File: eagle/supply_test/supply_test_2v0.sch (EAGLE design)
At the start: 46 parts, among them J1 SOCKET, J10 SOCKET, J11 SOCKET, J12 SOCKET, J13 SOCKET, J14 SOCKET, J15 SOCKET, J16 SOCKET, J17 SOCKET, J18 SOCKET, J19 SOCKET, J2 SOCKET, J20 SOCKET, J21 AC_INSW, J22 SOCKET, J23 MA02-1STR, J3 SOCKET, J4 SOCKET, J5 SOCKET, J6 SOCKET, J7 SOCKET, J8 SOCKET, J9 SOCKET

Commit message: supply test version 2
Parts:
- removed C4: (no value), rcl:C-EUC0603
- removed D4: ZENERBZT52, powerfilm:ZENERBZT52
- removed J23: MA02-1STR, con-lstb:MA02-1STR
- removed R7: 1k, rcl:R-US_R0603
- removed TP3: TP_STD, skyspecs:TP_STD
- added U1: TPS62122, powerfilm:TPS62122
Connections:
- removed net N$10: C4.1, D4.C, R7.2, TP3.P$1
- removed net N$9: J23.2, R7.1
- net GND: no longer C4.2, D4.A
- net VCC: no longer J23.1

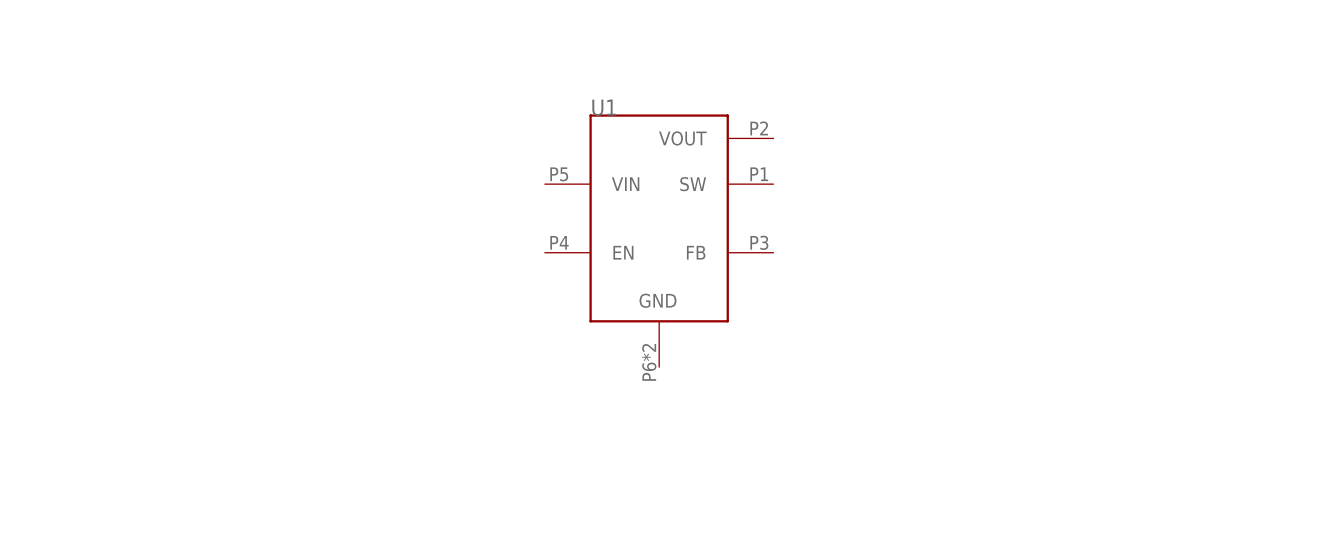
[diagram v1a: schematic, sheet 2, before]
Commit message: added different regulator to supply test
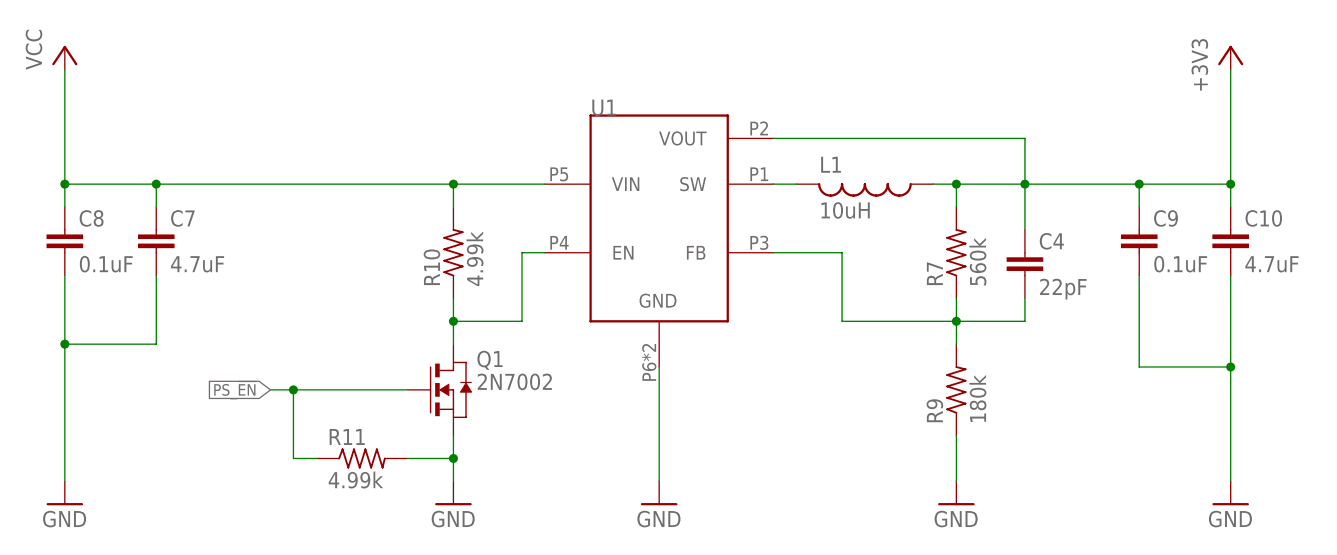
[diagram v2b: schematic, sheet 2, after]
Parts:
- added C10, C7: 4.7uF, rcl:C-EUC0603
- added C4: 22pF, rcl:C-EUC0603
- added C8, C9: 0.1uF, rcl:C-EUC0603
- added L1: 10uH, rcl:L-USL0805
- added Q1: 2N7002, nav:2N7002
- added R10, R11: 4.99k, rcl:R-US_R0603
- added R7: 560k, rcl:R-US_R0603
- added R9: 180k, rcl:R-US_R0603
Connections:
- new net +3V3: C10.1, C4.1, C9.1, L1.1, R7.2, U1.VOUT
- new net N$13: C4.2, R7.1, R9.2, U1.FB
- new net N$16: Q1.D, R10.1, U1.EN
- new net N$9: L1.2, U1.SW
- new net PS_!EN!: Q1.G, R11.1
- net GND: now also C10.2, C7.2, C8.2, C9.2, Q1.S, R11.2, R9.1, U1.GND
- net VCC: now also C7.1, C8.1, R10.2, U1.VIN
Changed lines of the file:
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@@
 <?xml version="1.0" encoding="utf-8"?>
 <!DOCTYPE eagle SYSTEM "eagle.dtd">
-<eagle version="6.5.0">
+<eagle version="6.3">
 <drawing>
 <settings>
@@
 </part>
 <part name="U1" library="powerfilm" deviceset="TPS62122" device=""/>
+<part name="L1" library="rcl" deviceset="L-US" device="L0805" value="10uH">
+<attribute name="DIGIKEY" value="490-4990-1-ND"/>
+</part>
+<part name="R7" library="rcl" deviceset="R-US_" device="R0603" value="560k"/>
+<part name="R9" library="rcl" deviceset="R-US_" device="R0603" value="180k"/>
+<part name="GND3" library="supply1" deviceset="GND" device=""/>
+<part name="GND4" library="supply1" deviceset="GND" device=""/>
+<part name="C4" library="rcl" deviceset="C-EU" device="C0603" value="22pF"/>
+<part name="R10" library="rcl" deviceset="R-US_" device="R0603" value="4.99k"/>
+<part name="Q1" library="nav" deviceset="2N7002" device=""/>
+<part name="GND5" library="supply1" deviceset="GND" device=""/>
+<part name="R11" library="rcl" deviceset="R-US_" device="R0603" value="4.99k"/>
+<part name="+3V1" library="supply1" deviceset="+3V3" device=""/>
+<part name="P+2" library="supply1" deviceset="VCC" device=""/>
+<part name="C7" library="rcl" deviceset="C-EU" device="C0603" value="4.7uF"/>
+<part name="C8" library="rcl" deviceset="C-EU" device="C0603" value="0.1uF"/>
+<part name="C9" library="rcl" deviceset="C-EU" device="C0603" value="0.1uF"/>
+<part name="C10" library="rcl" deviceset="C-EU" device="C0603" value="4.7uF"/>
+<part name="GND6" library="supply1" deviceset="GND" device=""/>
+<part name="GND7" library="supply1" deviceset="GND" device=""/>
 </parts>
 <sheets>
@@
 <instances>
 <instance part="U1" gate="G$1" x="0" y="0"/>
+<instance part="L1" gate="G$1" x="22.86" y="5.08" rot="R270">
+<attribute name="DIGIKEY" x="22.86" y="5.08" size="1.27" layer="96" rot="R270" display="off"/>
+</instance>
+<instance part="R7" gate="G$1" x="33.02" y="-2.54" rot="R90"/>
+<instance part="R9" gate="G$1" x="33.02" y="-17.78" rot="R90"/>
+<instance part="GND3" gate="1" x="33.02" y="-30.48"/>
+<instance part="GND4" gate="1" x="0" y="-30.48"/>
+<instance part="C4" gate="G$1" x="40.64" y="-2.54"/>
+<instance part="R10" gate="G$1" x="-22.86" y="-2.54" rot="R90"/>
+<instance part="Q1" gate="G$1" x="-22.86" y="-17.78"/>
+<instance part="GND5" gate="1" x="-22.86" y="-30.48"/>
+<instance part="R11" gate="G$1" x="-33.02" y="-25.4"/>
+<instance part="+3V1" gate="G$1" x="63.5" y="20.32"/>
+<instance part="P+2" gate="VCC" x="-66.04" y="20.32"/>
+<instance part="C7" gate="G$1" x="-55.88" y="0"/>
+<instance part="C8" gate="G$1" x="-66.04" y="0"/>
+<instance part="C9" gate="G$1" x="53.34" y="0"/>
+<instance part="C10" gate="G$1" x="63.5" y="0"/>
+<instance part="GND6" gate="1" x="-66.04" y="-30.48"/>
+<instance part="GND7" gate="1" x="63.5" y="-30.48"/>
 </instances>
 <busses>
 </busses>
 <nets>
+<net name="N$13" class="0">
+<segment>
+<pinref part="U1" gate="G$1" pin="FB"/>
+<wire x1="12.7" y1="-2.54" x2="20.32" y2="-2.54" width="0.1524" layer="91"/>
+<wire x1="20.32" y1="-2.54" x2="20.32" y2="-10.16" width="0.1524" layer="91"/>
+<pinref part="R7" gate="G$1" pin="1"/>
+<wire x1="20.32" y1="-10.16" x2="33.02" y2="-10.16" width="0.1524" layer="91"/>
+<wire x1="33.02" y1="-10.16" x2="33.02" y2="-7.62" width="0.1524" layer="91"/>
+<pinref part="R9" gate="G$1" pin="2"/>
+<wire x1="33.02" y1="-10.16" x2="33.02" y2="-12.7" width="0.1524" layer="91"/>
+<junction x="33.02" y="-10.16"/>
+<pinref part="C4" gate="G$1" pin="2"/>
+<wire x1="33.02" y1="-10.16" x2="40.64" y2="-10.16" width="0.1524" layer="91"/>
+<wire x1="40.64" y1="-10.16" x2="40.64" y2="-7.62" width="0.1524" layer="91"/>
+</segment>
+</net>
+<net name="GND" class="0">
+<segment>
+<pinref part="R9" gate="G$1" pin="1"/>
+<pinref part="GND3" gate="1" pin="GND"/>
+<wire x1="33.02" y1="-22.86" x2="33.02" y2="-27.94" width="0.1524" layer="91"/>
+</segment>
+<segment>
+<pinref part="U1" gate="G$1" pin="GND"/>
+<pinref part="GND4" gate="1" pin="GND"/>
+<wire x1="0" y1="-15.24" x2="0" y2="-27.94" width="0.1524" layer="91"/>
+</segment>
+<segment>
+<pinref part="Q1" gate="G$1" pin="S"/>
+<pinref part="GND5" gate="1" pin="GND"/>
+<wire x1="-22.86" y1="-22.86" x2="-22.86" y2="-25.4" width="0.1524" layer="91"/>
+<pinref part="R11" gate="G$1" pin="2"/>
+<wire x1="-22.86" y1="-25.4" x2="-22.86" y2="-27.94" width="0.1524" layer="91"/>
+<wire x1="-27.94" y1="-25.4" x2="-22.86" y2="-25.4" width="0.1524" layer="91"/>
+<junction x="-22.86" y="-25.4"/>
+</segment>
+<segment>
+<pinref part="C8" gate="G$1" pin="2"/>
+<pinref part="GND6" gate="1" pin="GND"/>
+<wire x1="-66.04" y1="-5.08" x2="-66.04" y2="-12.7" width="0.1524" layer="91"/>
+<pinref part="C7" gate="G$1" pin="2"/>
+<wire x1="-66.04" y1="-12.7" x2="-66.04" y2="-27.94" width="0.1524" layer="91"/>
+<wire x1="-55.88" y1="-5.08" x2="-55.88" y2="-12.7" width="0.1524" layer="91"/>
+<wire x1="-55.88" y1="-12.7" x2="-66.04" y2="-12.7" width="0.1524" layer="91"/>
+<junction x="-66.04" y="-12.7"/>
+</segment>
+<segment>
+<pinref part="C9" gate="G$1" pin="2"/>
+<wire x1="53.34" y1="-5.08" x2="53.34" y2="-15.24" width="0.1524" layer="91"/>
+<pinref part="C10" gate="G$1" pin="2"/>
+<wire x1="53.34" y1="-15.24" x2="63.5" y2="-15.24" width="0.1524" layer="91"/>
+<wire x1="63.5" y1="-15.24" x2="63.5" y2="-5.08" width="0.1524" layer="91"/>
+<pinref part="GND7" gate="1" pin="GND"/>
+<wire x1="63.5" y1="-15.24" x2="63.5" y2="-27.94" width="0.1524" layer="91"/>
+<junction x="63.5" y="-15.24"/>
+</segment>
+</net>
+<net name="N$16" class="0">
+<segment>
+<pinref part="R10" gate="G$1" pin="1"/>
+<wire x1="-22.86" y1="-7.62" x2="-22.86" y2="-10.16" width="0.1524" layer="91"/>
+<wire x1="-22.86" y1="-10.16" x2="-15.24" y2="-10.16" width="0.1524" layer="91"/>
+<wire x1="-15.24" y1="-10.16" x2="-15.24" y2="-2.54" width="0.1524" layer="91"/>
+<pinref part="U1" gate="G$1" pin="EN"/>
+<wire x1="-15.24" y1="-2.54" x2="-12.7" y2="-2.54" width="0.1524" layer="91"/>
+<pinref part="Q1" gate="G$1" pin="D"/>
+<wire x1="-22.86" y1="-10.16" x2="-22.86" y2="-12.7" width="0.1524" layer="91"/>
+<junction x="-22.86" y="-10.16"/>
+</segment>
+</net>
+<net name="PS_!EN!" class="0">
+<segment>
+<pinref part="R11" gate="G$1" pin="1"/>
+<wire x1="-38.1" y1="-25.4" x2="-40.64" y2="-25.4" width="0.1524" layer="91"/>
+<wire x1="-40.64" y1="-25.4" x2="-40.64" y2="-17.78" width="0.1524" layer="91"/>
+<pinref part="Q1" gate="G$1" pin="G"/>
+<wire x1="-40.64" y1="-17.78" x2="-27.94" y2="-17.78" width="0.1524" layer="91"/>
+<wire x1="-43.18" y1="-17.78" x2="-40.64" y2="-17.78" width="0.1524" layer="91"/>
+<junction x="-40.64" y="-17.78"/>
+<label x="-43.18" y="-17.78" size="1.27" layer="95" rot="R180" xref="yes"/>
+</segment>
+</net>
+<net name="N$9" class="0">
+<segment>
+<pinref part="U1" gate="G$1" pin="SW"/>
+<pinref part="L1" gate="G$1" pin="2"/>
+<wire x1="12.7" y1="5.08" x2="15.24" y2="5.08" width="0.1524" layer="91"/>
+</segment>
+</net>
+<net name="VCC" class="0">
+<segment>
+<pinref part="P+2" gate="VCC" pin="VCC"/>
+<pinref part="C8" gate="G$1" pin="1"/>
+<wire x1="-66.04" y1="17.78" x2="-66.04" y2="5.08" width="0.1524" layer="91"/>
+<pinref part="U1" gate="G$1" pin="VIN"/>
+<pinref part="R10" gate="G$1" pin="2"/>
+<wire x1="-66.04" y1="5.08" x2="-66.04" y2="2.54" width="0.1524" layer="91"/>
+<wire x1="-12.7" y1="5.08" x2="-22.86" y2="5.08" width="0.1524" layer="91"/>
+<wire x1="-22.86" y1="5.08" x2="-22.86" y2="2.54" width="0.1524" layer="91"/>
+<wire x1="-22.86" y1="5.08" x2="-55.88" y2="5.08" width="0.1524" layer="91"/>
+<junction x="-22.86" y="5.08"/>
+<junction x="-66.04" y="5.08"/>
+<pinref part="C7" gate="G$1" pin="1"/>
+<wire x1="-55.88" y1="5.08" x2="-66.04" y2="5.08" width="0.1524" layer="91"/>
+<wire x1="-55.88" y1="2.54" x2="-55.88" y2="5.08" width="0.1524" layer="91"/>
+<junction x="-55.88" y="5.08"/>
+</segment>
+</net>
+<net name="+3V3" class="0">
+<segment>
+<pinref part="U1" gate="G$1" pin="VOUT"/>
+<pinref part="C4" gate="G$1" pin="1"/>
+<wire x1="12.7" y1="10.16" x2="40.64" y2="10.16" width="0.1524" layer="91"/>
+<wire x1="40.64" y1="10.16" x2="40.64" y2="5.08" width="0.1524" layer="91"/>
+<wire x1="40.64" y1="5.08" x2="40.64" y2="0" width="0.1524" layer="91"/>
+<junction x="40.64" y="5.08"/>
+<pinref part="R7" gate="G$1" pin="2"/>
+<wire x1="33.02" y1="5.08" x2="40.64" y2="5.08" width="0.1524" layer="91"/>
+<wire x1="33.02" y1="2.54" x2="33.02" y2="5.08" width="0.1524" layer="91"/>
+<pinref part="L1" gate="G$1" pin="1"/>
+<wire x1="30.48" y1="5.08" x2="33.02" y2="5.08" width="0.1524" layer="91"/>
+<junction x="33.02" y="5.08"/>
+<pinref part="C10" gate="G$1" pin="1"/>
+<wire x1="40.64" y1="5.08" x2="53.34" y2="5.08" width="0.1524" layer="91"/>
+<wire x1="53.34" y1="5.08" x2="63.5" y2="5.08" width="0.1524" layer="91"/>
+<wire x1="63.5" y1="5.08" x2="63.5" y2="2.54" width="0.1524" layer="91"/>
+<pinref part="+3V1" gate="G$1" pin="+3V3"/>
+<wire x1="63.5" y1="5.08" x2="63.5" y2="17.78" width="0.1524" layer="91"/>
+<junction x="63.5" y="5.08"/>
+<pinref part="C9" gate="G$1" pin="1"/>
+<wire x1="53.34" y1="5.08" x2="53.34" y2="2.54" width="0.1524" layer="91"/>
+<junction x="53.34" y="5.08"/>
+</segment>
+</net>
 </nets>
 </sheet>

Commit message: miniaturized power supply
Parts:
- removed C2: (no value), rcl:C-EUC0805
- removed C5: (no value), SparkFun-Passives:CAP_POL1206
- removed C6: (no value), rcl:C-USC1210
- removed F1: 80mA FAST, powerfilm:FUSE
- removed J1, J10, J11, J12, J13, J14, J15, J16, J17, J18, J19, J2, J20, J22, J3, J4, J5, J6, J7, J8, J9: SOCKET, powerfilm:SOCKET
- removed RV1: 275VAC, powerfilm:MOV_CU4032
- R2, R3: DIGIKEY P0.0GCT-ND -> (none)
- R4, R5, R6: value 0 -> NP; DIGIKEY P0.0GCT-ND -> (none)
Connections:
- removed net N$11: F1.P1, J21.P
- removed net N$12: J16.P1, J17.P1, R3.1, R4.2
- removed net N$14: F1.P2, J20.P1, R5.1, RV1.P2
- removed net N$15: J18.P1, J19.P1, R4.1, R5.2
- net GND: no longer C2.2, C5.-, C6.2, J10.P1, J12.P1
- net N$1: no longer J2.P1, J3.P1
- net N$2: no longer J1.P1, RV1.P1
- net N$3: now also D1.A, D2.C, R2.2; no longer C1.1, J4.P1, J5.P1, R6.1, R8.2
- net N$4: now also C1.1, R2.1, R4.1, R8.2; no longer D1.A, D2.C, J6.P1, J9.P1, R6.2
- net N$5: now also D3.P4, R4.2; no longer D1.C, J15.P1, J7.P1, R2.1, R3.2
- net N$6: now also J21.P, R3.1, R6.1; no longer D3.P2, J13.P1
- net N$7: now also R5.1; no longer J22.P1
- net N$8: now also D3.P2, R6.2; no longer D3.P4, J14.P1
- net VCC: now also D1.C, R3.2, R5.2; no longer C2.1, C5.+, C6.1, J11.P1, J8.P1, R2.2
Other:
- note added: "Populate R4, R5, & R6 with 0ohm"
- note added: "Remove R2 and R3"
- note added: "Replace D2 with 0ohm"
- note added: "To Make Full Wave:"
- moved on the sheet: D3, R2, R3, R4, R5, R6
